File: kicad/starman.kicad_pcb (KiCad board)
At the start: 4 copper layers, 182 x 150 mm, 202 parts, among them J1 M20-8771246, J10 Barrel_Jack_MountingPin, J2 M20-8770646, J3 M20-8771246, J4 ESW-106-44-T-S, J5 Conn_02x03_Counter_Clockwise, J6 ESW-112-44-T-S, J7 Conn_01x10, J8 ESW-112-44-T-S, J9 Conn_01x10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

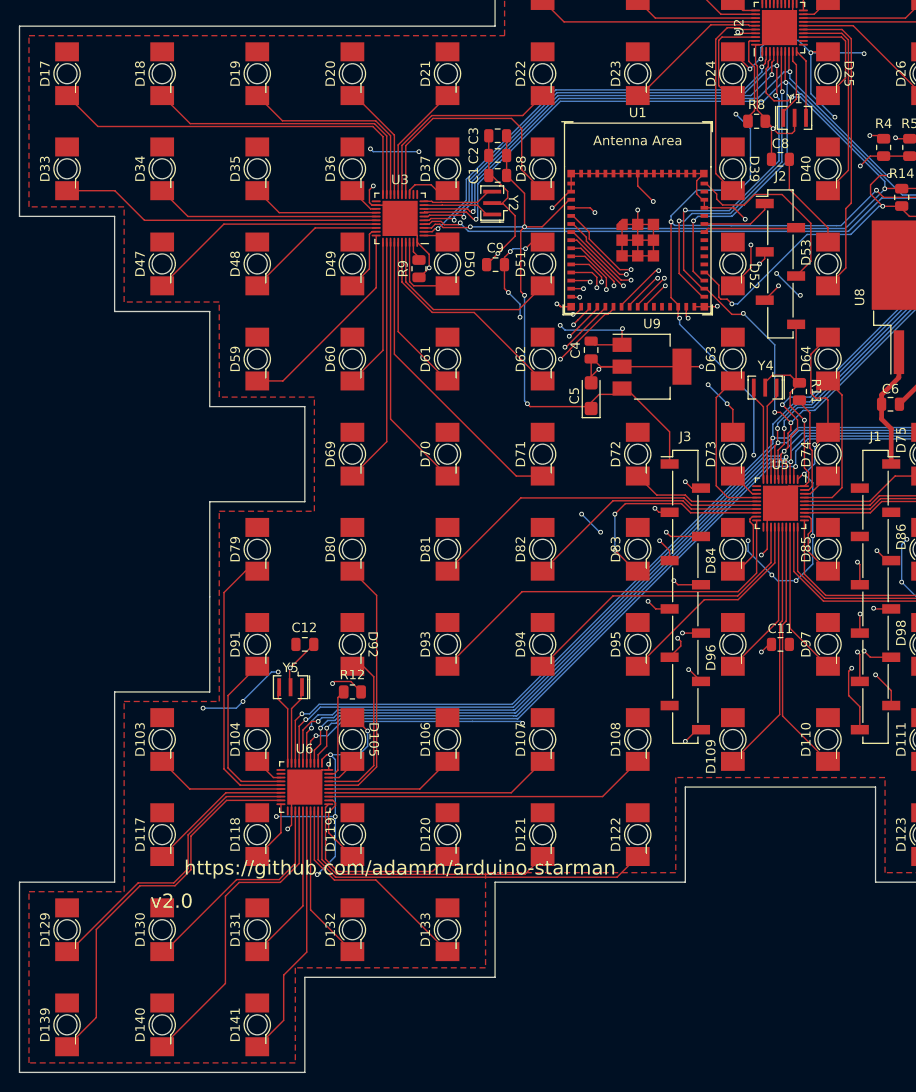
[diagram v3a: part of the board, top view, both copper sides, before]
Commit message: Fixed DRC, restored logos, fixed github url
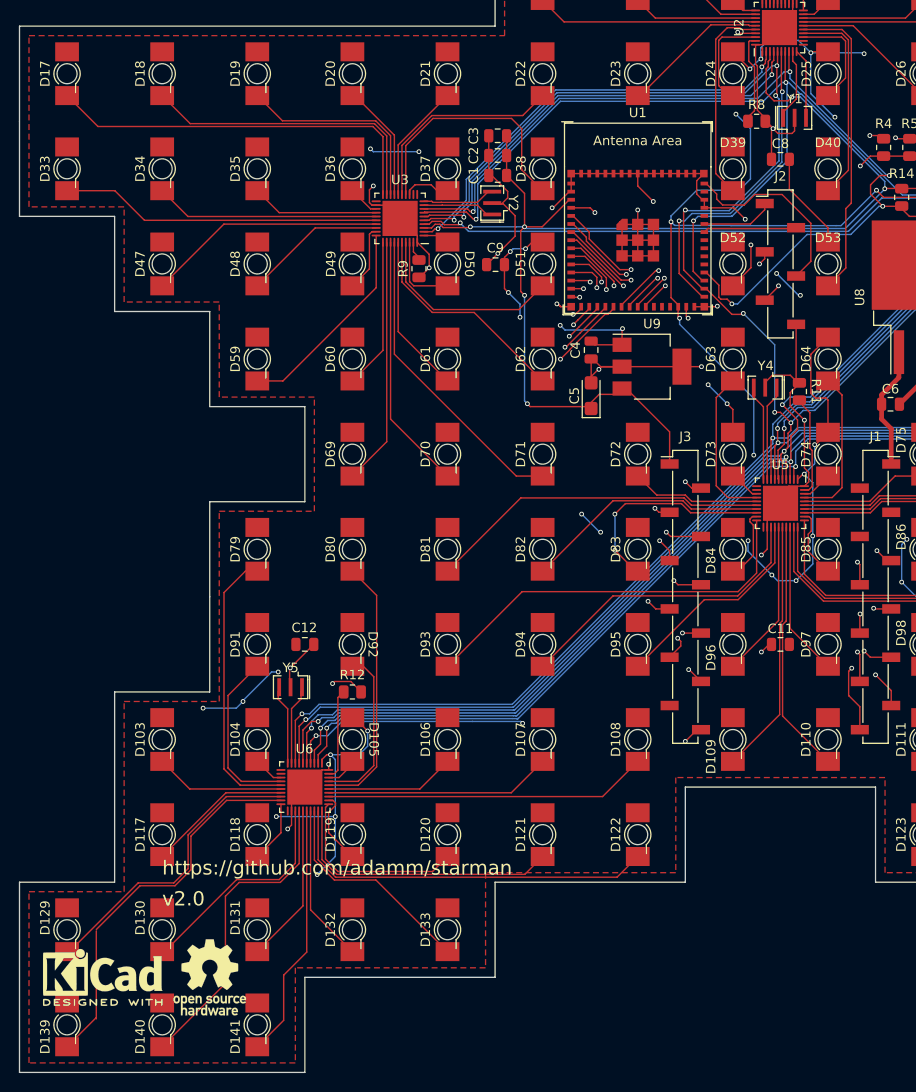
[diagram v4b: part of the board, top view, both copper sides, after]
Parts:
- added REF**: OSHW-Logo_7.5x8mm_SilkScreen, Symbol:OSHW-Logo_7.5x8mm_SilkScreen, F.Cu at (50.0, 170.0)
- added REF**: KiCad-Logo2_5mm_SilkScreen, Symbol:KiCad-Logo2_5mm_SilkScreen, F.Cu at (38.8, 170.0)
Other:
- board text added: "https://github.com/adamm/starman"
- board text removed: "https://github.com/adamm/arduino-starman"
